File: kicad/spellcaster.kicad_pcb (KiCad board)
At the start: 4 copper layers, 10 x 61 mm, 52 parts, among them U1 nRF52820-QDxx, U2 LSM6DSL, Y1 32k, Y2 Crystal_GND24

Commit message: Silkscreen + stitching
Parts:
- removed H1: MountingHole, MountingHole:MountingHole_2.2mm_M2_Pad_Via
- moved kibuzzard-64E668FF 2.10 mm to (52.7, 132.6)
- moved kibuzzard-64E66915 2.10 mm to (57.5, 132.6)
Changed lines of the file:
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@@
   )
   (footprint "kibuzzard-64E66915" (layer "F.Cu")
-    (at 57.5056 134.6708)
+    (at 57.5056 132.569702)
     (descr "Generated with KiBuzzard")
     (tags "kb_params=eyJBbGlnbm1lbnRDaG9pY2UiOiAiTGVmdCIsICJDYXBMZWZ0Q2hvaWNlIjogIiIsICJDYXBSaWdodENob2ljZSI6ICIpIiwgIkZvbnRDb21ib0JveCI6ICJVYnVudHVNb25vLUIiLCAiSGVpZ2h0Q3RybCI6ICIyIiwgIkxheWVyQ29tYm9Cb3giOiAiRi5TaWxrUyIsICJNdWx0aUxpbmVUZXh0IjogIi0iLCAiUGFkZGluZ0JvdHRvbUN0cmwiOiAiNSIsICJQYWRkaW5nTGVmdEN0cmwiOiAiMiIsICJQYWRkaW5nUmlnaHRDdHJsIjogIjIiLCAiUGFkZGluZ1RvcEN0cmwiOiAiNSIsICJXaWR0aEN0cmwiOiAiIn0=")
@@
   )
   (footprint "kibuzzard-64E668FF" (layer "F.Cu")
-    (at 52.6796 134.6708)
+    (at 52.6796 132.569702)
     (descr "Generated with KiBuzzard")
     (tags "kb_params=eyJBbGlnbm1lbnRDaG9pY2UiOiAiTGVmdCIsICJDYXBMZWZ0Q2hvaWNlIjogIiIsICJDYXBSaWdodENob2ljZSI6ICIpIiwgIkZvbnRDb21ib0JveCI6ICJVYnVudHVNb25vLUIiLCAiSGVpZ2h0Q3RybCI6ICIyIiwgIkxheWVyQ29tYm9Cb3giOiAiRi5TaWxrUyIsICJNdWx0aUxpbmVUZXh0IjogIisiLCAiUGFkZGluZ0JvdHRvbUN0cmwiOiAiNSIsICJQYWRkaW5nTGVmdEN0cmwiOiAiMiIsICJQYWRkaW5nUmlnaHRDdHJsIjogIjIiLCAiUGFkZGluZ1RvcEN0cmwiOiAiNSIsICJXaWR0aEN0cmwiOiAiIn0=")
@@
       (stroke (width 0) (type solid)) (fill solid) (layer "F.SilkS"))
   )
-  (footprint "MountingHole:MountingHole_2.2mm_M2_Pad_Via" (layer "F.Cu")
-    (at 64.041 26.44)
-    (descr "Mounting Hole 2.2mm, M2")
-    (tags "mounting hole 2.2mm m2")
-    (property "Sheetfile" "spellcaster.kicad_sch")
-    (property "Sheetname" "")
-    (property "exclude_from_bom" "")
-    (property "ki_description" "Mounting Hole without connection")
-    (property "ki_keywords" "mounting hole")
-    (attr exclude_from_pos_files exclude_from_bom)
-    (fp_text reference "H1" (at 0 -3.2) (layer "F.SilkS") hide
-        (effects (font (size 1 1) (thickness 0.15)))
-    )
-    (fp_text value "MountingHole" (at 0 3.2) (layer "F.Fab") hide
-        (effects (font (size 1 1) (thickness 0.15)))
-    )
-    (fp_text user "${REFERENCE}" (at 0 0) (layer "F.Fab")
-        (effects (font (size 1 1) (thickness 0.15)))
-    )
-    (fp_circle (center 0 0) (end 2.2 0)
-      (stroke (width 0.15) (type solid)) (fill none) (layer "Cmts.User"))
-    (fp_circle (center 0 0) (end 2.45 0)
-      (stroke (width 0.05) (type solid)) (fill none) (layer "F.CrtYd"))
-    (pad "1" thru_hole circle (at -1.65 0) (size 0.7 0.7) (drill 0.4) (layers "*.Cu" "*.Mask"))
-    (pad "1" thru_hole circle (at -1.166726 -1.166726) (size 0.7 0.7) (drill 0.4) (layers "*.Cu" "*.Mask"))
-    (pad "1" thru_hole circle (at -1.166726 1.166726) (size 0.7 0.7) (drill 0.4) (layers "*.Cu" "*.Mask"))
-    (pad "1" thru_hole circle (at 0 -1.65) (size 0.7 0.7) (drill 0.4) (layers "*.Cu" "*.Mask"))
-    (pad "1" thru_hole circle (at 0 0) (size 4.4 4.4) (drill 2.2) (layers "*.Cu" "*.Mask"))
-    (pad "1" thru_hole circle (at 0 1.65) (size 0.7 0.7) (drill 0.4) (layers "*.Cu" "*.Mask"))
-    (pad "1" thru_hole circle (at 1.166726 -1.166726) (size 0.7 0.7) (drill 0.4) (layers "*.Cu" "*.Mask"))
-    (pad "1" thru_hole circle (at 1.166726 1.166726) (size 0.7 0.7) (drill 0.4) (layers "*.Cu" "*.Mask"))
-    (pad "1" thru_hole circle (at 1.65 0) (size 0.7 0.7) (drill 0.4) (layers "*.Cu" "*.Mask"))
-  )
   (footprint "kibuzzard-64E66855" (layer "B.Cu")

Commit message: Add vibration motor
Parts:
- removed kibuzzard-64E66C17: G***, kibuzzard-64E66C17
- added D2: 1N4148W, Diode_SMD:D_SOD-123, F.Cu at (55.8, 119.9)
- added M1: Motor_DC, TestPoint:TestPoint_2Pads_Pitch2.54mm_Drill0.8mm, F.Cu at (58.4, 120.8)
- added Q1: 2N7002, Package_TO_SOT_SMD:SOT-23, F.Cu at (52.6, 119.9)
- added R4: 10k, Resistor_SMD:R_0402_1005Metric, F.Cu at (51.6, 117.6)
- added kibuzzard-64E7045C: G***, kibuzzard-64E7045C, F.Cu at (53.0, 78.0)
- added kibuzzard-64E704EF: G***, kibuzzard-64E704EF, F.Cu at (59.5, 122.0)
- added kibuzzard-64E70501: G***, kibuzzard-64E70501, F.Cu at (59.5, 117.0)
- added kibuzzard-64E70567: G***, kibuzzard-64E70567, F.Cu at (51.9, 129.4)
- added kibuzzard-64E7057C: G***, kibuzzard-64E7057C, F.Cu at (58.2, 129.3)
- kibuzzard-64E667F3: moved to B.Cu
- moved S1 7.49 mm to (58.0, 125.8), turned to 90 degrees
- moved kibuzzard-64E667F3 4.15 mm to (51.5, 119.9), turned to 90 degrees
- moved kibuzzard-64E66B38 4.00 mm to (55.0, 127.0)
- moved S2 2.92 mm to (51.9, 125.8), turned to 90 degrees
- moved kibuzzard-64E66855 1.25 mm to (54.4, 119.9), turned to 90 degrees
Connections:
- U1 pad 22: unconnected-(U1-P0.16-Pad22) -> VIB
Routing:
- net VIB: track 0.00 -> 20.7 mm, vias 0 -> 3
- net Net-(D2-A): track 0.00 -> 9.00 mm
- net RST: track 36.3 -> 43.3 mm
- net VDD: track 19.0 -> 21.0 mm, vias 7 -> 9
- net BTN_A: track 23.4 -> 24.9 mm
- net GND: track 16.8 -> 17.9 mm, vias 19 -> 24

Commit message: Fixes vibration motor routing
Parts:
- removed kibuzzard-64E7045C: G***, kibuzzard-64E7045C
- added kibuzzard-64E705F6: G***, kibuzzard-64E705F6, F.Cu at (52.5, 77.1)
- added kibuzzard-64E7063C: G***, kibuzzard-64E7063C, F.Cu at (53.2, 78.9)
- moved S1 0.50 mm to (58.0, 125.3)
- moved S2 0.50 mm to (51.9, 125.3)
- moved kibuzzard-64E70567 0.50 mm to (51.9, 128.9)
- moved kibuzzard-64E7057C 0.40 mm to (58.2, 128.9)
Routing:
- net VIB: track 20.7 -> 22.3 mm
- net Net-(D2-A): track 9.00 -> 8.42 mm
- net RST: track 43.3 -> 43.8 mm
- net BTN_A: track 24.9 -> 25.4 mm
- net GND: vias 24 -> 26

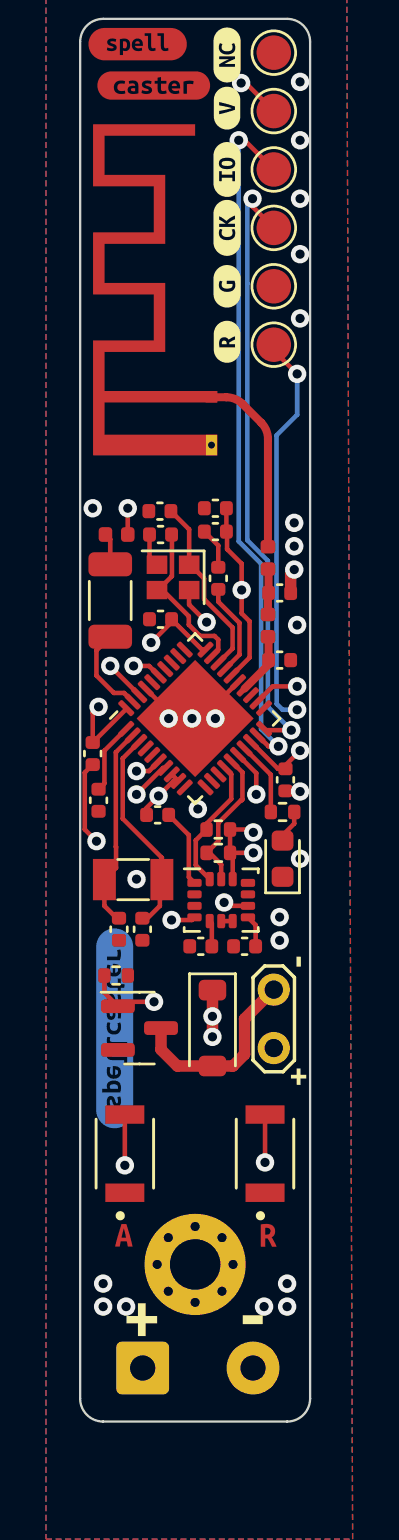
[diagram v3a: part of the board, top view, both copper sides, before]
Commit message: Add optional CR2032 holder
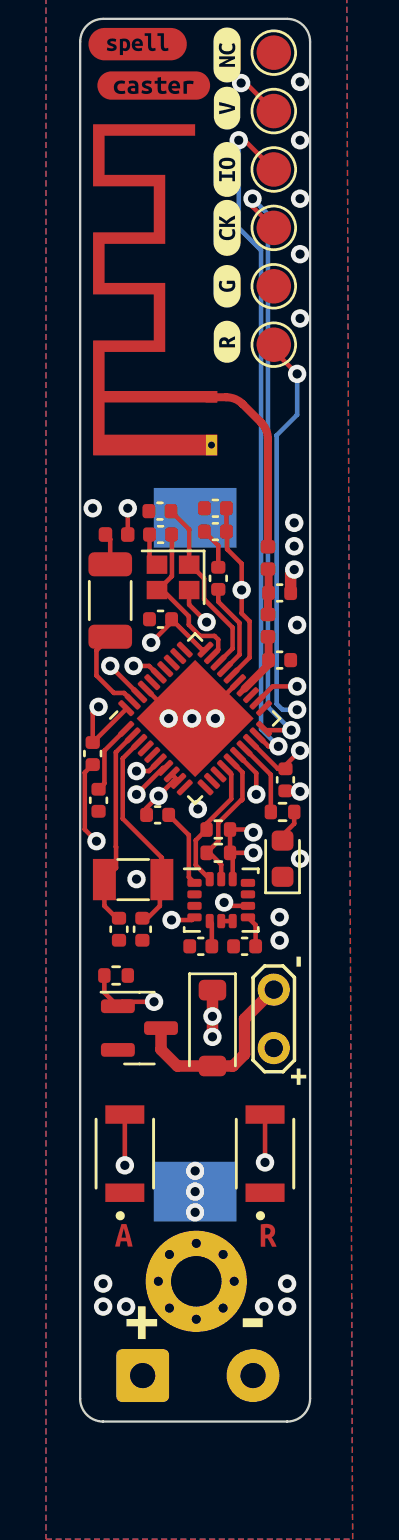
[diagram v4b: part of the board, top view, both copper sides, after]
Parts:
- removed kibuzzard-64E667F3: G***, kibuzzard-64E667F3
- added BT2: CR2032, Battery:BatteryHolder_Keystone_1060_1x2032, B.Cu at (55.0, 112.3)
- added kibuzzard-64E668FF: G***, kibuzzard-64E668FF, B.Cu at (52.7, 132.7)
- added kibuzzard-64E668FF: G***, kibuzzard-64E668FF, B.Cu at (51.9, 127.8)
- added kibuzzard-64E66915: G***, kibuzzard-64E66915, B.Cu at (57.5, 132.7)
- added kibuzzard-64E70B5B: G***, kibuzzard-64E70B5B, B.Cu at (52.9, 89.1)
- added kibuzzard-64E70C98: G***, kibuzzard-64E70C98, B.Cu at (51.9, 96.4)
- BT1: value Battery_Cell -> Through holes
- moved kibuzzard-64E66B38 38.1 mm to (54.7, 88.9), turned to 90 degrees
- moved kibuzzard-64E66855 31.1 mm to (51.3, 89.0)
- moved H2 0.73 mm to (55.0, 130.9)
- moved BT1 0.33 mm to (52.7, 135.0)
- moved kibuzzard-64E668FF 0.13 mm to (52.7, 132.7)
- moved kibuzzard-64E66915 0.13 mm to (57.5, 132.7)
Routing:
- net VDD: vias 9 -> 12

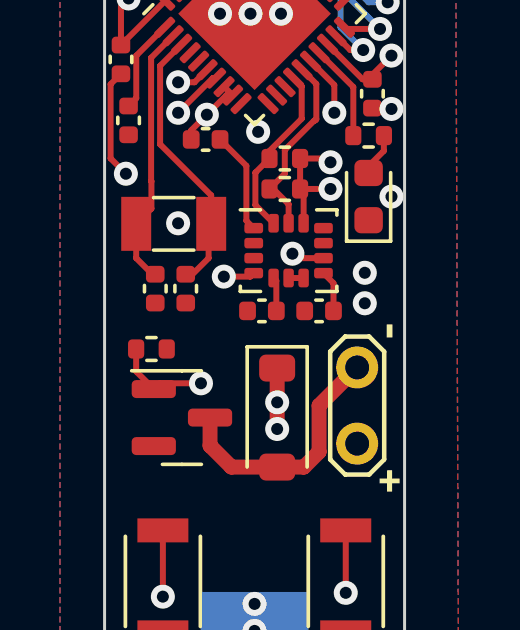
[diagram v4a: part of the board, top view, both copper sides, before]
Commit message: Fixed missing accel vcc connection
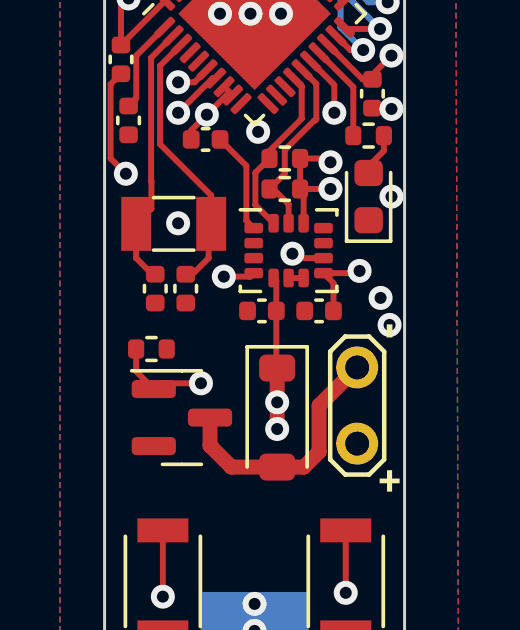
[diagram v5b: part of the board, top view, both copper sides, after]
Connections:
- C14 pad 2: Net-(U2-VDDIO) -> VDD
- C16 pad 2: Net-(U2-VDD) -> VDD
- TP6 pad 1: GPIO -> unconnected-(TP6-Pad1)
- U2 pad 5: Net-(U2-VDDIO) -> VDD
- U2 pad 8: Net-(U2-VDD) -> VDD
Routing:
- net VDD: track 21.0 -> 26.7 mm, vias 12 -> 13
- net Net-(U2-VDD): track 1.40 -> 0.00 mm
- net Net-(U2-VDDIO): track 1.13 -> 0.00 mm
